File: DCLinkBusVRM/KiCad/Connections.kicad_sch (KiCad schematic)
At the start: 15 parts, among them J1 1987724, J2 1987724, J3 Conn_Coaxial, J4 Conn_Coaxial, J5 Conn_01x02_Pin, J6 Conn_01x02_Pin, M1 Fan_4pin

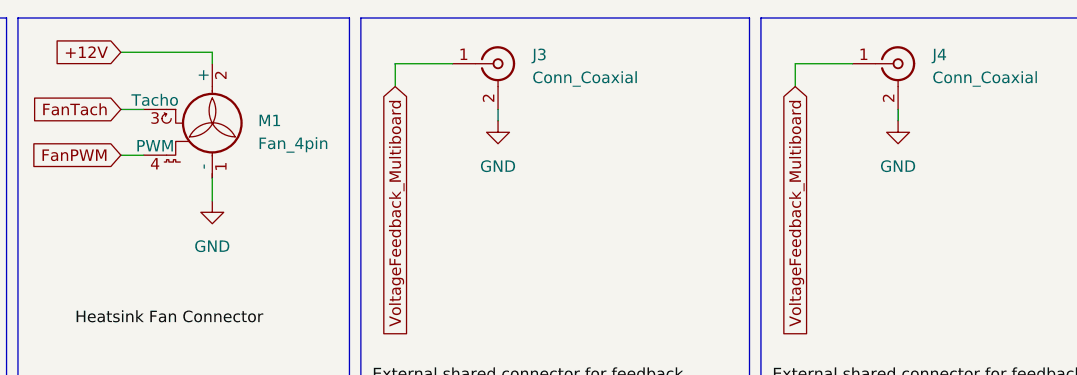
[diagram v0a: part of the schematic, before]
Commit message: Update boost converter, add dynamic brake grid, etc
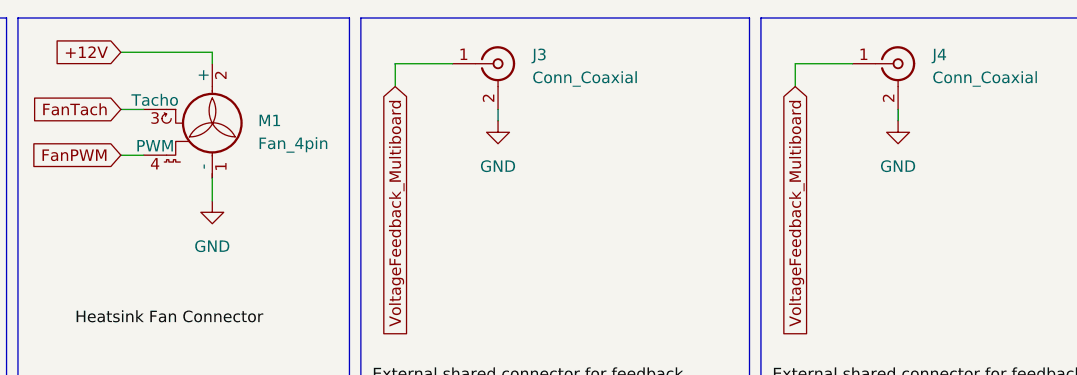
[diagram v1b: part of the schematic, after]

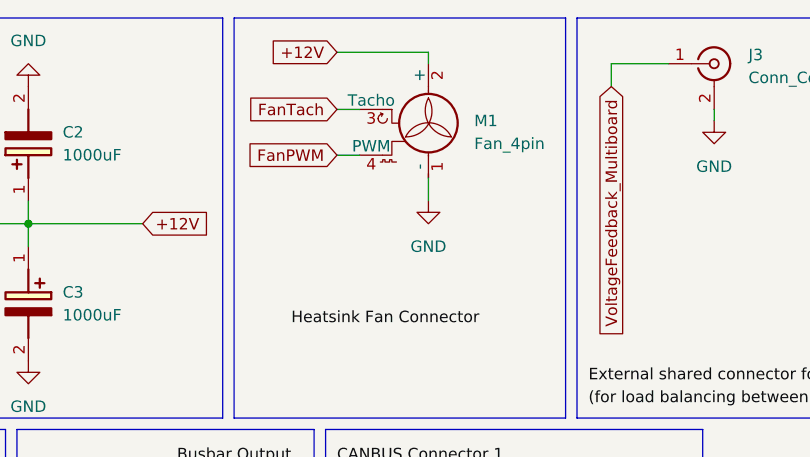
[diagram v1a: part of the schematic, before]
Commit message: Update Canbus protocol for vrm
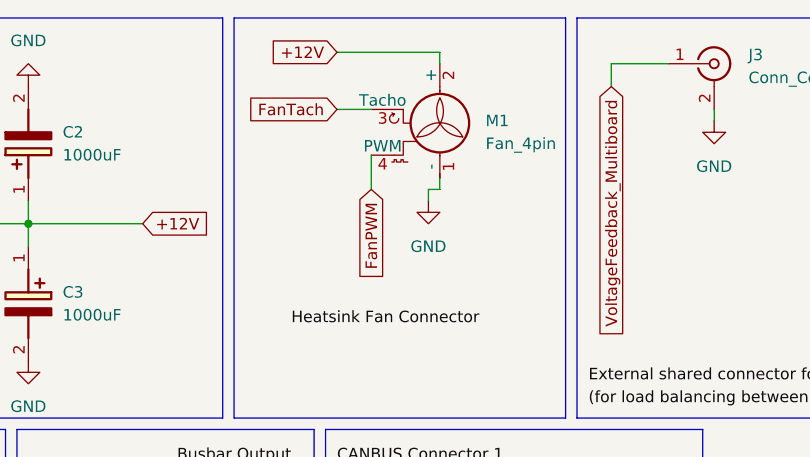
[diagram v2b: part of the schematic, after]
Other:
- moved on the sheet: M1
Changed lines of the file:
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@@
+	(wire
+		(pts
+			(xy 93.98 33.02) (xy 93.98 29.21)
+		)
+		(stroke
+			(width 0)
+			(type default)
+		)
+	)
 	(wire
 		(pts
@@
 	(wire
 		(pts
-			(xy 90.17 24.13) (xy 92.71 24.13)
-		)
-		(stroke
-			(width 0)
-			(type default)
-		)
-	)
-	(wire
-		(pts
-			(xy 100.33 17.78) (xy 100.33 19.05)
+			(xy 101.6 33.02) (xy 100.33 33.02)
+		)
+		(stroke
+			(width 0)
+			(type default)
+		)
+	)
+	(wire
+		(pts
+			(xy 90.17 24.13) (xy 93.98 24.13)
+		)
+		(stroke
+			(width 0)
+			(type default)
+		)
+	)
+	(wire
+		(pts
+			(xy 101.6 17.78) (xy 101.6 19.05)
 		)
 		(stroke
@@
 	(wire
 		(pts
-			(xy 90.17 17.78) (xy 100.33 17.78)
-		)
-		(stroke
-			(width 0)
-			(type default)
-		)
-	)
-	(wire
-		(pts
-			(xy 100.33 31.75) (xy 100.33 34.29)
+			(xy 90.17 17.78) (xy 101.6 17.78)
+		)
+		(stroke
+			(width 0)
+			(type default)
+		)
+	)
+	(wire
+		(pts
+			(xy 101.6 31.75) (xy 101.6 33.02)
 		)
 		(stroke
@@
 	(wire
 		(pts
+			(xy 100.33 33.02) (xy 100.33 34.29)
+		)
+		(stroke
+			(width 0)
+			(type default)
+		)
+	)
+	(wire
+		(pts
 			(xy 67.31 87.63) (xy 69.85 87.63)
 		)
@@
 		(pts
 			(xy 120.65 19.05) (xy 127 19.05)
-		)
-		(stroke
-			(width 0)
-			(type default)
-		)
-	)
-	(wire
-		(pts
-			(xy 90.17 29.21) (xy 92.71 29.21)
 		)
 		(stroke
@@
 	(global_label "FanPWM"
 		(shape input)
-		(at 90.17 29.21 180)
-		(fields_autoplaced yes)
-		(effects
-			(font
-				(size 1.27 1.27)
-			)
-			(justify right)
-		)
-		(property "Intersheetrefs" "${INTERSHEET_REFS}"
-			(at 79.6254 29.21 0)
+		(at 93.98 33.02 270)
+		(fields_autoplaced yes)
+		(effects
+			(font
+				(size 1.27 1.27)
+			)
+			(justify right)
+		)
+		(property "Intersheetrefs" "${INTERSHEET_REFS}"
+			(at 93.98 43.5646 90)
 			(effects
 				(font
@@
 	(symbol
 		(lib_id "Motor:Fan_4pin")
-		(at 100.33 26.67 0)
+		(at 101.6 26.67 0)
 		(unit 1)
 		(exclude_from_sim no)
@@
 		(fields_autoplaced yes)
 		(property "Reference" "M1"
-			(at 105.41 25.3999 0)
+			(at 106.68 25.3999 0)
 			(effects
 				(font
@@
 		)
 		(property "Value" "Fan_4pin"
-			(at 105.41 27.9399 0)
+			(at 106.68 27.9399 0)
 			(effects
 				(font
@@
 		)
 		(property "Footprint" "Connector:FanPinHeader_1x04_P2.54mm_Vertical"
-			(at 100.33 26.416 0)
+			(at 101.6 26.416 0)
 			(effects
 				(font
@@
 		)
 		(property "Datasheet" "http://www.formfactors.org/developer%5Cspecs%5Crev1_2_public.pdf"
-			(at 100.33 26.416 0)
+			(at 101.6 26.416 0)
 			(effects
 				(font
@@
 		)
 		(property "Description" "Fan, tacho output, PWM input, 4-pin connector"
-			(at 100.33 26.67 0)
-			(effects
-				(font
+			(at 101.6 26.67 0)
+			(effects
+				(font
